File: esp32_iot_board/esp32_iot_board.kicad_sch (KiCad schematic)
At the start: 45 parts, among them J1 USB_C_Receptacle_USB2.0, J2 Conn_01x04, J3 Screw_Terminal_01x03, J4 Screw_Terminal_01x08, J5 Screw_Terminal_01x02, K1 RT314A05, Q1 UMH3N, Q2 BC817, SW1 SW_SPST, U1 ESP32-WROOM-32D, U2 USBLC6-2P6, U3 CP2104, U4 Si7020-A20, U5 74HC245, U6 TLV1117LV-3.3

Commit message: 1.09hr
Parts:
- added C10, C12, C13, C14: 100nf, symbol Device:C_Small
- added C11: 22u, symbol Device:C_Small
- added C15: 22uf, symbol Device:C_Small
- added R11, R14: 10k, symbol Device:R_Small
- added R12, R13: 4k7, symbol Device:R_Small
- added R15, R16: 1k, symbol Device:R_Small
- added R17, R18, R19, R20: 22R, symbol Device:R_Small
- C1: value C_Polarized_Small -> 1000u/25V
- D2: value LED -> YELLOW
- U5: value 74HC245 -> 74AHCT245
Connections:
- net +3V3: now also J2.2 (Pin_2), U1.2 (VDD), U4.5 (VDD), C11.1, C12.1, C14.1, C15.1, R11.1, R12.1, R13.1
- net +5V: now also D1.1 (K), K1.A1, U5.1 (A->B), U5.20 (VCC), C13.1, R16.1
- net EN: now also U1.3 (EN), C10.1, R11.2
- net GND: now also C1.2, J2.1 (Pin_1), J4.7 (Pin_7), J4.8 (Pin_8), J5.2 (Pin_2), Q2.2 (E), U4.2 (GND), U4.7 (PAD), U5.10 (GND), U5.19 (CE), U5.6 (A4), U5.7 (A5), U5.8 (A6), U5.9 (A7), C10.2, C11.2, C12.2, C13.2, C14.2, C15.2, R14.2
- net IO0: now also U1.25 (IO0)
- net SDA: now reaches J2.3 (Pin_3)
- net SDA: now also U4.1 (SDA), R12.2
- net SCL: now reaches J2.4 (Pin_4)
- net SCL: now also U4.6 (SCL), R13.2
- net at D1.2 (A): now also D2.1 (K), K1.A2, Q2.3 (C)
- net at F1.1: now also C1.1, J5.1 (Pin_1)
- net at F1.2: now also J4.1 (Pin_1), J4.2 (Pin_2)
- net at J4.3 (Pin_3): now also R17.2
- net at J4.4 (Pin_4): now also R18.2
- net at J4.5 (Pin_5): now also R19.2
- net at J4.6 (Pin_6): now also R20.2
- net at D2.2 (A): now also R16.2
- net at J3.1 (Pin_1): now also K1.12
- net at J3.2 (Pin_2): now also K1.11
- net at J3.3 (Pin_3): now also K1.14
- net at Q2.1 (B): now also R14.1, R15.2
- net at U5.15 (B3): now also R20.1
- net at U5.16 (B2): now also R19.1
- net at U5.17 (B1): now also R18.1
- net at U5.18 (B0): now also R17.1
- net LEDSTR1: now reaches U5.2 (A0)
- net LEDSTR2: now reaches U5.3 (A1)
- net LEDSTR3: now reaches U5.4 (A2)
- net LEDSTR4: now reaches U5.5 (A3)
- new net RELAY: R15.1
- no-connect marks 0 -> 4
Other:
- note added: "GND"
- note added: "OWIIC"
- note added: "SCL"
- note added: "SDA"
- note added: "VCC"
- moved on the sheet: C1, D1, D2, F1, J3, J4, J5, K1, Q2, U4, U5

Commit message: 1.30 min
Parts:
- added J6: Conn_02x05_Odd_Even, symbol Connector_Generic:Conn_02x05_Odd_Even
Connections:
- net +3V3: now also J6.1 (Pin_1), J6.2 (Pin_2)
- net GND: now also U1.1 (GND), U1.15 (GND), U1.38 (GND), U1.39 (GND), J6.10 (Pin_10), J6.9 (Pin_9)
- net LEDSTR1: now also U1.27 (IO16)
- net LEDSTR2: now also U1.28 (IO17)
- net LEDSTR3: now also U1.30 (IO18)
- net LEDSTR4: now also U1.31 (IO19)
- net LED_B: now also U1.13 (IO14)
- net LED_G: now also U1.23 (IO15)
- net LED_R: now also U1.16 (IO13)
- net RELAY: now also U1.10 (IO25)
- net RX: now also U1.34 (RXD0/IO3)
- net SCL: now also U1.37 (IO23)
- net SDA: now also U1.36 (IO22)
- net SW: now also U1.33 (IO21)
- net TX: now also U1.35 (TXD0/IO1)
- net GPIO26: now reaches U1.11 (IO26)
- net GPIO26: now also J6.3 (Pin_3)
- net GPIO27: now reaches U1.12 (IO27)
- net GPIO27: now also J6.5 (Pin_5)
- net GPIO34: now reaches U1.6 (IO34)
- net GPIO34: now also J6.6 (Pin_6)
- net GPIO35: now reaches U1.7 (IO35)
- net GPIO35: now also J6.8 (Pin_8)
- net GPIO32: now reaches U1.8 (IO32)
- net GPIO32: now also J6.7 (Pin_7)
- net GPIO33: now reaches U1.9 (IO33)
- net GPIO33: now also J6.4 (Pin_4)
- no-connect marks 4 -> 16
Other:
- note added: "I2C Sensor + OWIIC Connector"
- note added: "LD0 5V to 3.3V"
- note added: "LED Driver"
- note added: "MCU"
- note added: "Mounting"
- note added: "Power + Programming Interface"
- note added: "Relay"
- note added: "USER I/O"
- moved on the sheet: C1, C10, C13, C14, C15, C2, C3, C4, C5, C6, C7, C8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

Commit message: 1.35 -> footprints assigned
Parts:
- C1: footprint (none) -> Capacitor_THT:C_Radial_D10.0mm_H12.5mm_P5.00mm
- C10, C11, C12, C13, C14, C15, C2, C3, C4, C5, C6, C7, C8, C9: footprint (none) -> Capacitor_SMD:C_1206_3216Metric
- D2, D4: footprint (none) -> LED_SMD:LED_1206_3216Metric
- D3: footprint (none) -> LED_SMD:LED_RGB_Wuerth-PLCC4_3.2x2.8mm_150141M173100
- F1, F2: footprint (none) -> Fuse:Fuse_1206_3216Metric_Pad1.42x1.75mm_HandSolder
- FB1: footprint (none) -> Inductor_SMD:L_0603_1608Metric_Pad1.05x0.95mm_HandSolder
- H1, H2, H3, H4: footprint (none) -> MountingHole:MountingHole_3.2mm_M3_Pad_Via
- J1: footprint (none) -> Connector_USB:USB_C_Receptacle_HRO_TYPE-C-31-M-12
- J2: footprint (none) -> Connector_JST:JST_SH_SM04B-SRSS-TB_1x04-1MP_P1.00mm_Horizontal
- J3: footprint (none) -> TerminalBlock_Phoenix:TerminalBlock_Phoenix_PT-1,5-3-5.0-H_1x03_P5.00mm_Horizontal
- J4: footprint (none) -> TerminalBlock_Phoenix:TerminalBlock_Phoenix_PT-1,5-8-5.0-H_1x08_P5.00mm_Horizontal
- J5: footprint (none) -> TerminalBlock_Phoenix:TerminalBlock_Phoenix_MKDS-3-3-5.08_1x03_P5.08mm_Horizontal
- J6: footprint (none) -> Connector_PinHeader_2.54mm:PinHeader_2x05_P2.54mm_Vertical
- R1, R10, R11, R12, R13, R14, R15, R16, R17, R18, R19, R2, R20, R3, R4, R5, R6, R7, R8, R9: footprint (none) -> Resistor_SMD:R_1206_3216Metric
- SW1: footprint (none) -> Button_Switch_SMD:SW_Push_1P1T_NO_6x6mm_H9.5mm
- U5: footprint (none) -> Package_DIP:DIP-20_W7.62mm

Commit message: prog routed
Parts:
- removed C1: 1000u/25V, Capacitor_THT:C_Radial_D10.0mm_H12.5mm_P5.00mm, symbol Device:C_Polarized_Small
- removed C11: 22u, Capacitor_SMD:C_1206_3216Metric, symbol Device:C_Small
- removed C12, C13: 100nf, Capacitor_SMD:C_1206_3216Metric, symbol Device:C_Small
- removed D1: LL4148, Diode_SMD:D_MiniMELF, symbol Diode:LL4148
- removed D2: YELLOW, LED_SMD:LED_1206_3216Metric, symbol Device:LED
- removed F1: Fuse, Fuse:Fuse_1206_3216Metric_Pad1.42x1.75mm_HandSolder, symbol Device:Fuse
- removed J2: Conn_01x04, Connector_JST:JST_SH_SM04B-SRSS-TB_1x04-1MP_P1.00mm_Horizontal, symbol Connector_Generic:Conn_01x04
- removed J3: Screw_Terminal_01x03, TerminalBlock_Phoenix:TerminalBlock_Phoenix_PT-1,5-3-5.0-H_1x03_P5.00mm_Horizontal, symbol Connector:Screw_Terminal_01x03
- removed J4: Screw_Terminal_01x08, TerminalBlock_Phoenix:TerminalBlock_Phoenix_PT-1,5-8-5.0-H_1x08_P5.00mm_Horizontal, symbol Connector:Screw_Terminal_01x08
- removed J5: Screw_Terminal_01x02, TerminalBlock_Phoenix:TerminalBlock_Phoenix_MKDS-3-3-5.08_1x03_P5.08mm_Horizontal, symbol Connector:Screw_Terminal_01x02
- removed K1: RT314A05, Relay_THT:Relay_SPDT_Schrack-RT1-16A-FormC_RM5mm, symbol Relay:RT314A05
- removed Q2: BC817, Package_TO_SOT_SMD:SOT-23, symbol Transistor_BJT:BC817
- removed R12, R13: 4k7, Resistor_SMD:R_1206_3216Metric, symbol Device:R_Small
- removed R14: 10k, Resistor_SMD:R_1206_3216Metric, symbol Device:R_Small
- removed R15, R16: 1k, Resistor_SMD:R_1206_3216Metric, symbol Device:R_Small
- removed R17, R18, R19, R20: 22R, Resistor_SMD:R_1206_3216Metric, symbol Device:R_Small
- removed U4: Si7020-A20, Package_DFN_QFN:DFN-6-1EP_3x3mm_P1mm_EP1.5x2.4mm, symbol Sensor_Humidity:Si7020-A20
- removed U5: 74AHCT245, Package_DIP:DIP-20_W7.62mm, symbol 74xx:74HC245
- added J2: Screw_Terminal_01x02, TerminalBlock_Phoenix:TerminalBlock_Phoenix_PT-1,5-2-5.0-H_1x02_P5.00mm_Horizontal, symbol Connector:Screw_Terminal_01x02
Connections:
- net +5V: now also U2.5 (VBUS)
- net +5VP: now also J2.2 (Pin_2)
- net GND: now also J2.1 (Pin_1)
- net at J1.A7 (D-), J1.B7 (D-): now also U2.3 (I/O2); no longer U2.1 (I/O1)
- net at J1.A6 (D+), J1.B6 (D+): now also U2.1 (I/O1); no longer U2.3 (I/O2)
- net at U2.4 (I/O2): now also U3.4 (D-); no longer U3.3 (D+)
- net at U2.6 (I/O1): now also U3.3 (D+); no longer U3.4 (D-)
- no-connect marks 16 -> 23
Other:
- note removed: "GND"
- note removed: "I2C Sensor + OWIIC Connector"
- note removed: "LED Driver"
- note removed: "OWIIC"
- note removed: "Relay"
- note removed: "SCL"
- note removed: "SDA"
- note removed: "VCC"

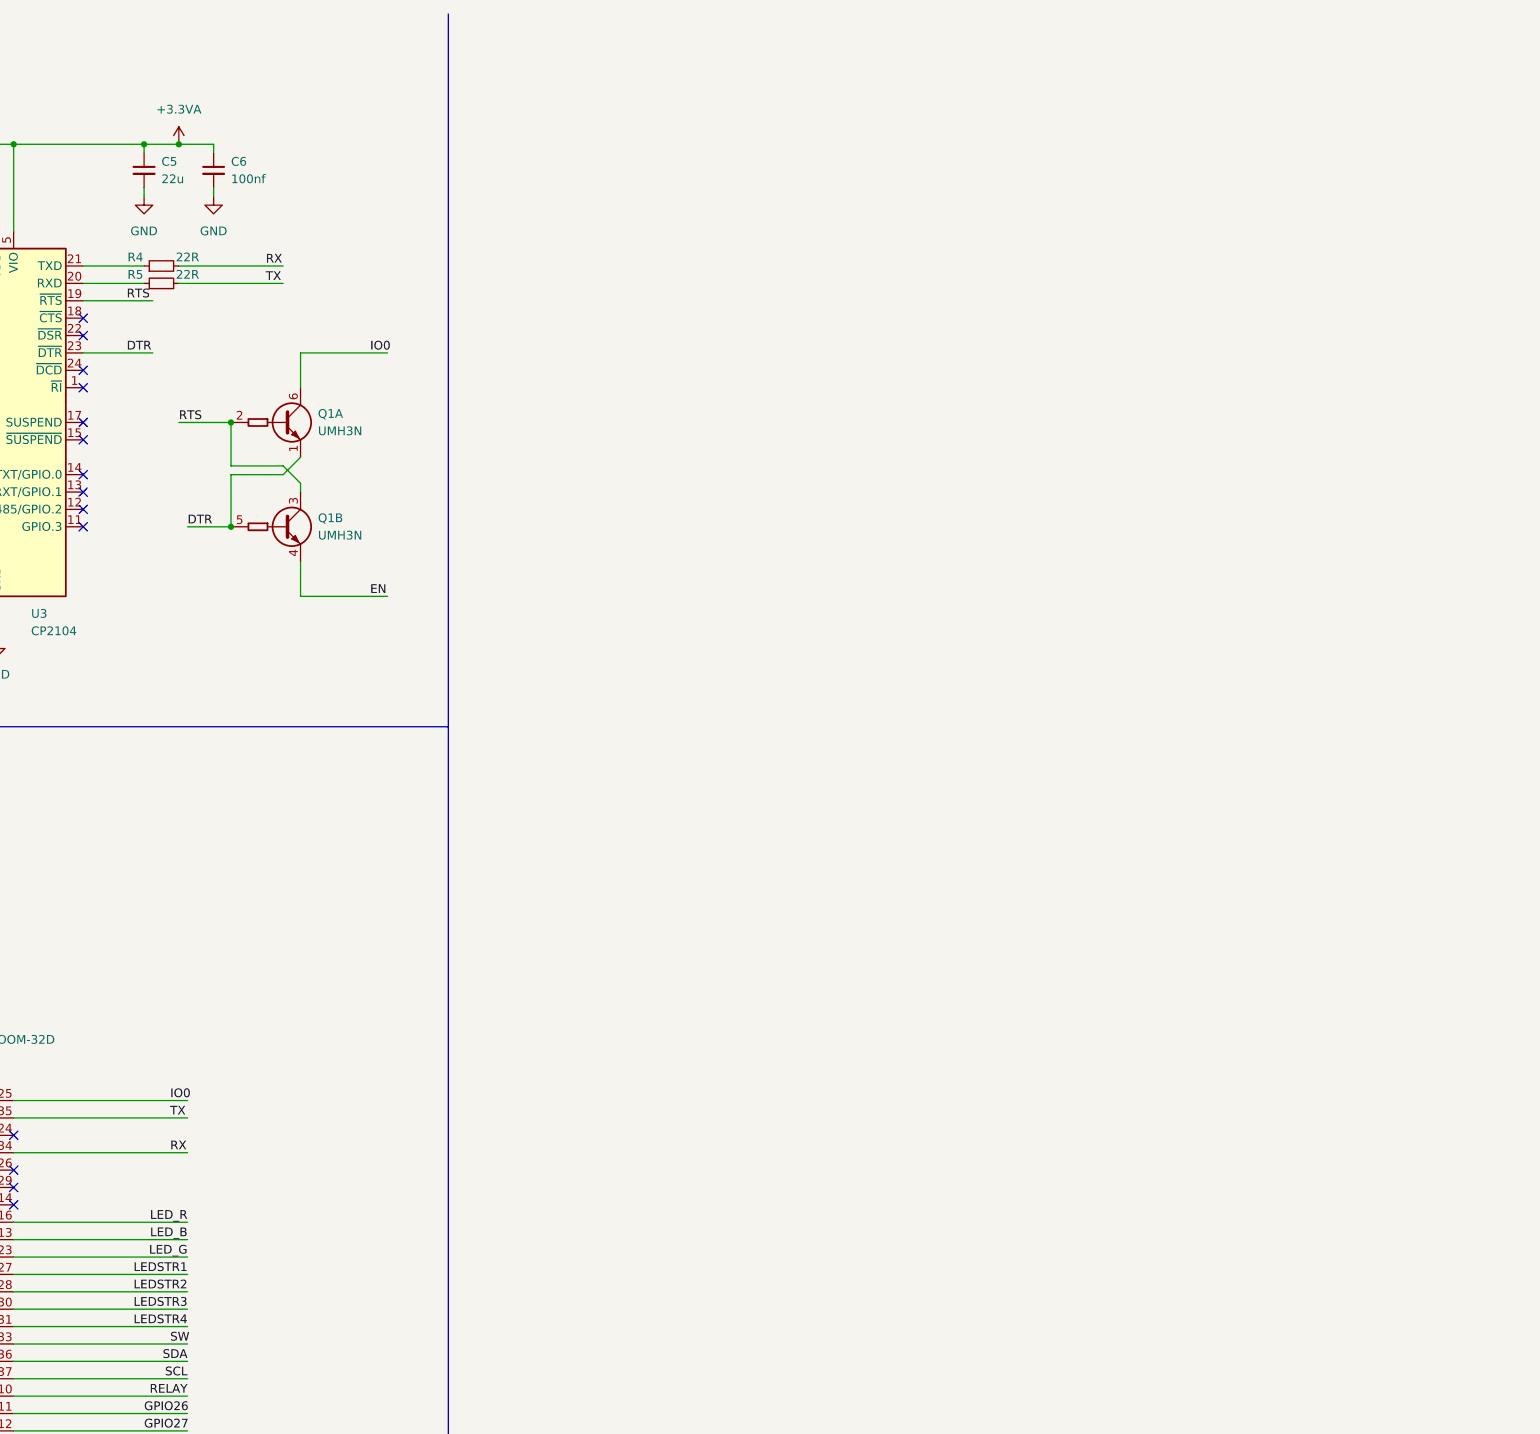
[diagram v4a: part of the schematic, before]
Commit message: added i2c and onewire
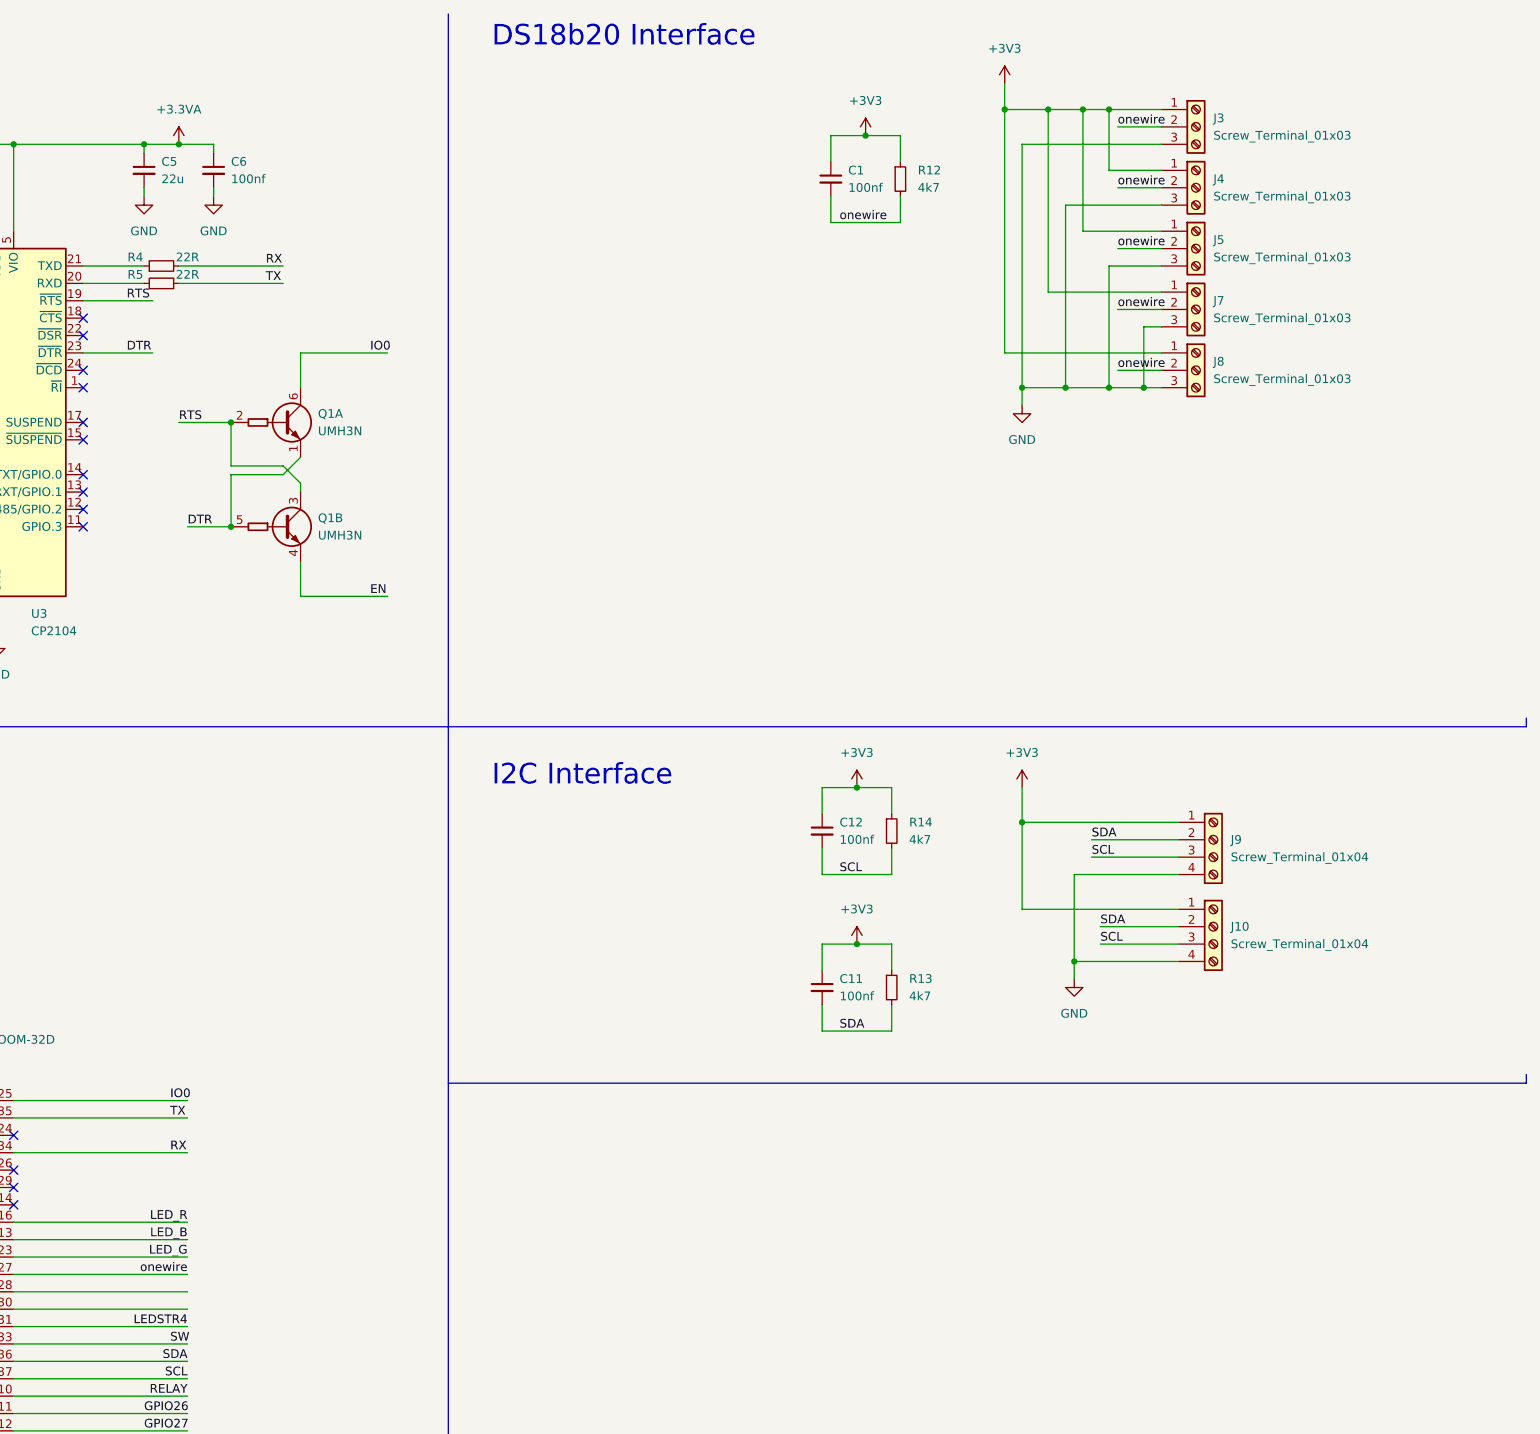
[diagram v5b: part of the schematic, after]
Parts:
- added C1, C11, C12: 100nf, Capacitor_SMD:C_1206_3216Metric, symbol Device:C_Small
- added J10, J9: Screw_Terminal_01x04, TerminalBlock_Phoenix:TerminalBlock_Phoenix_MKDS-3-4-5.08_1x04_P5.08mm_Horizontal, symbol Connector:Screw_Terminal_01x04
- added J3, J4, J5, J7, J8: Screw_Terminal_01x03, TerminalBlock_Phoenix:TerminalBlock_Phoenix_MKDS-3-3-5.08_1x03_P5.08mm_Horizontal, symbol Connector:Screw_Terminal_01x03
- added R12, R13, R14: 4k7, Resistor_SMD:R_1206_3216Metric, symbol Device:R_Small
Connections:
- net +3V3: now also C1.1, C11.1, C12.1, J10.1 (Pin_1), J3.1 (Pin_1), J4.1 (Pin_1), J5.1 (Pin_1), J7.1 (Pin_1), J8.1 (Pin_1), J9.1 (Pin_1), R12.1, R13.1, R14.1
- net GND: now also J10.4 (Pin_4), J3.3 (Pin_3), J4.3 (Pin_3), J5.3 (Pin_3), J7.3 (Pin_3), J8.3 (Pin_3), J9.4 (Pin_4)
- net SCL: now also C12.2, J10.3 (Pin_3), J9.3 (Pin_3), R14.2
- net SDA: now also C11.2, J10.2 (Pin_2), J9.2 (Pin_2), R13.2
- net LEDSTR1 renamed onewire
- net onewire: now also C1.2, J3.2 (Pin_2), J4.2 (Pin_2), J5.2 (Pin_2), J7.2 (Pin_2), J8.2 (Pin_2), R12.2
- net LEDSTR2: no longer names the net of U1.28 (IO17)
- net LEDSTR3: no longer names the net of U1.30 (IO18)
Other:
- note added: "DS18b20 Interface"
- note added: "I2C Interface"
